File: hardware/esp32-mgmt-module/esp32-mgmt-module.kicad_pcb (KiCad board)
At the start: 4 copper layers, 77 x 31.8 mm, 93 parts, among them J1 Bus_PCI_Express_x1, J2 BOOT, J3 RJ45_Hanrun_HR913550A_Horizon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, J4 GPIO, J5 SWD, J6 USB_C, J7 UART, Q1 MMBT3904, Q2 MMBT3904, SW1 RESET, U1 RTL8201F-VB-CG, U2 74LVC1G14, U3 AMS1117-3.3, U4 ESP32-WROOM-32E, U5 CH9102F, Y1 25MHz

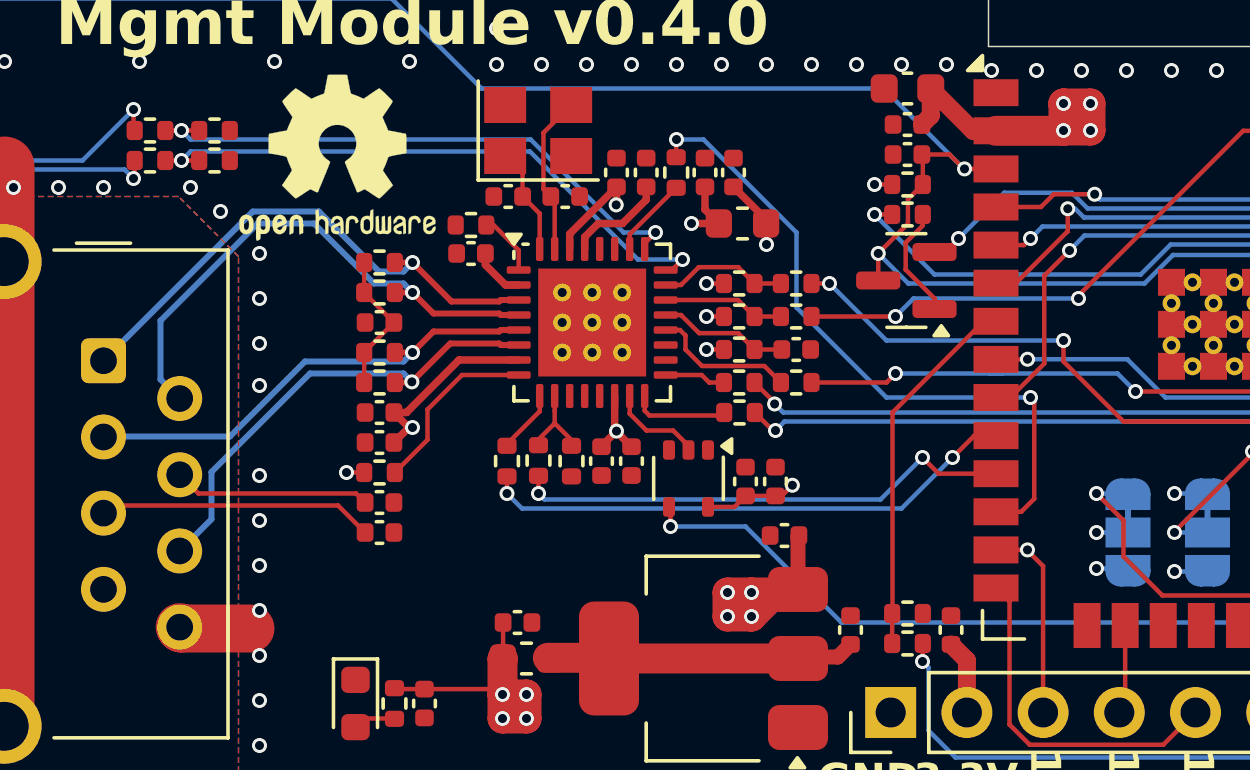
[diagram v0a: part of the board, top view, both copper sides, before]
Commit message: fix: connect gpio12 to phyrstb
fix: switch to 50mhz phy xtal
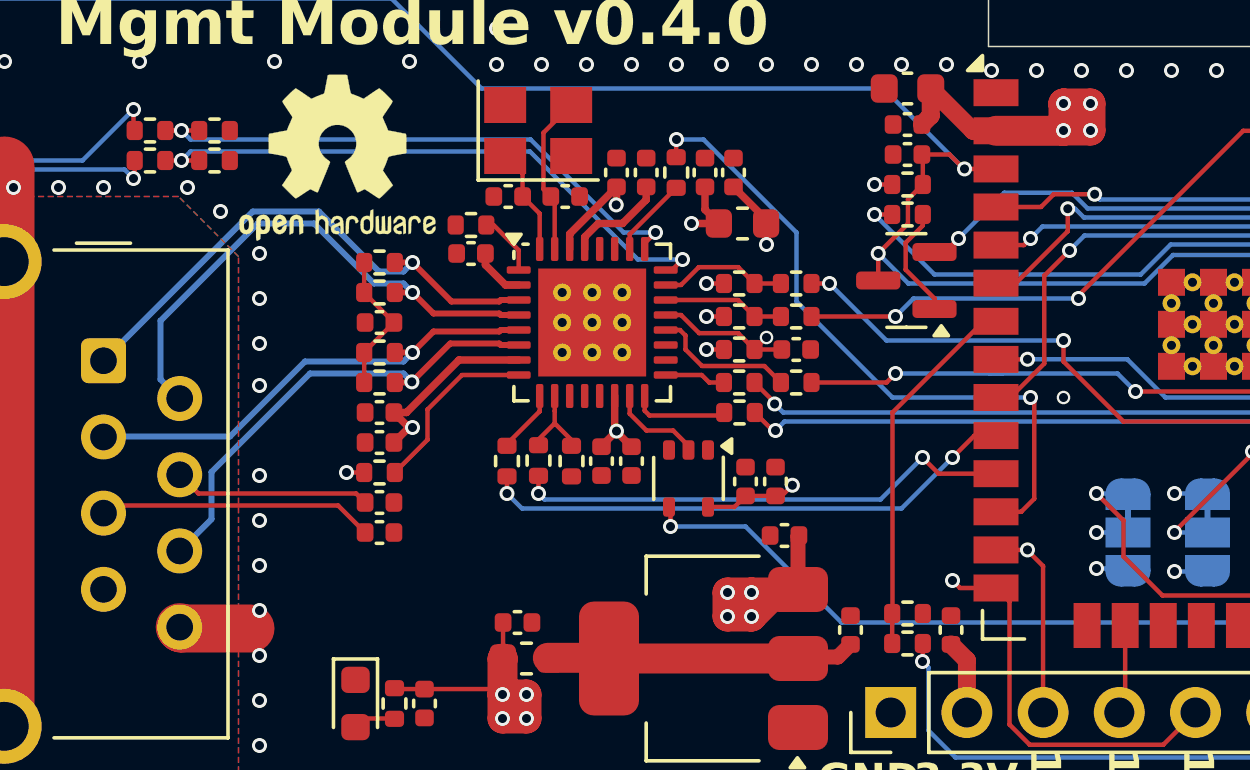
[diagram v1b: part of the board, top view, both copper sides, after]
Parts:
- Y1: value 25MHz -> 50MHz
- renumbered C11 to C10, C24 to C11, C13 to C12, C14 to C13, C9 to C14, C16 to C15, C12 to C16, C18 to C17, C19 to C18, C15 to C19, C17 to C21, C21 to C23, C26 to C24, C30 to C25, C31 to C26, C32 to C27, C33 to C28, C34 to C29, C35 to C30, C10 to C9, D4 to D2, D2 to D3, R26 to R22, R22 to R23, R23 to R24, R24 to R25, R25 to R26, R36 to R31, R31 to R32, R32 to R33, R33 to R34, R34 to R35, R35 to R36
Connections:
- C3 pad 1: Net-(U1-~{PHYRSTB}) -> /GPIO12
- R2 pad 2: Net-(U1-~{PHYRSTB}) -> /GPIO12
- U1 pad 21: Net-(U1-~{PHYRSTB}) -> /GPIO12
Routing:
- net /GPIO12: track 11.7 -> 28.8 mm, vias 0 -> 2
- net Net-(U1-~{PHYRSTB}): track 4.35 -> 0.00 mm
- net GND: vias 139 -> 140
